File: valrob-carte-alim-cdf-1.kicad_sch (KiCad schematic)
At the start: 0 parts

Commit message: schem: add ESP32-S3-WROOM-1 MCU
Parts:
- added C5: 1u, Capacitor_SMD:C_0402_1005Metric, symbol Device:C
- added C6: 22u, Capacitor_SMD:C_0603_1608Metric, symbol Device:C
- added C7: 0u1, Capacitor_SMD:C_0402_1005Metric, symbol Device:C
- added J4, J6: Conn_01x04_Pin, Connector_PinHeader_2.54mm:PinHeader_1x04_P2.54mm_Vertical, symbol Connector:Conn_01x04_Pin
- added R6, R7: 10k, Resistor_SMD:R_0402_1005Metric, symbol Device:R
- added R8, R9: 22, Resistor_SMD:R_0402_1005Metric, symbol Device:R
- added U4: ESP32-S3-WROOM-1, PCM_Espressif:ESP32-S3-WROOM-1, symbol PCM_Espressif:ESP32-S3-WROOM-1
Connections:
- new net: J4.1 (Pin_1), U4.32 (MTCK/GPIO39/CLK_OUT3/SUBSPICS1)
- new net: J4.2 (Pin_2), U4.33 (MTDO/GPIO40/CLK_OUT2)
- new net: J4.3 (Pin_3), U4.34 (MTDI/GPIO41/CLK_OUT1)
- new net: J4.4 (Pin_4), U4.35 (MTMS/GPIO42)
- new net +3V3: C6.1, C7.1, J6.1 (Pin_1), R6.2, R7.2, U4.2 (3V3)
- new net BOOT: R7.1, U4.27 (GPIO0/BOOT)
- new net CHIP_PU: C5.2, R6.1, U4.3 (EN)
- new net D+: R8.2
- new net D-: R9.2
- new net ESP_D+: R8.1, U4.14 (GPIO20/U1CTS/ADC2_CH9/CLK_OUT1/USB_D+)
- new net ESP_D-: R9.1, U4.13 (GPIO19/U1RTS/ADC2_CH8/CLK_OUT2/USB_D-)
- new net GND: C5.1, C6.2, C7.2, J6.3 (Pin_3), U4.1 (GND), U4.40 (GND), U4.41 (GND)
- new net U0RXD: J6.2 (Pin_2), U4.36 (U0RXD/GPIO44/CLK_OUT2)
- new net U0TXD: J6.4 (Pin_4), U4.37 (U0TXD/GPIO43/CLK_OUT1)
- no-connect marks 0 -> 9
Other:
- note added: "EN RC delay"
- note added: "UART"

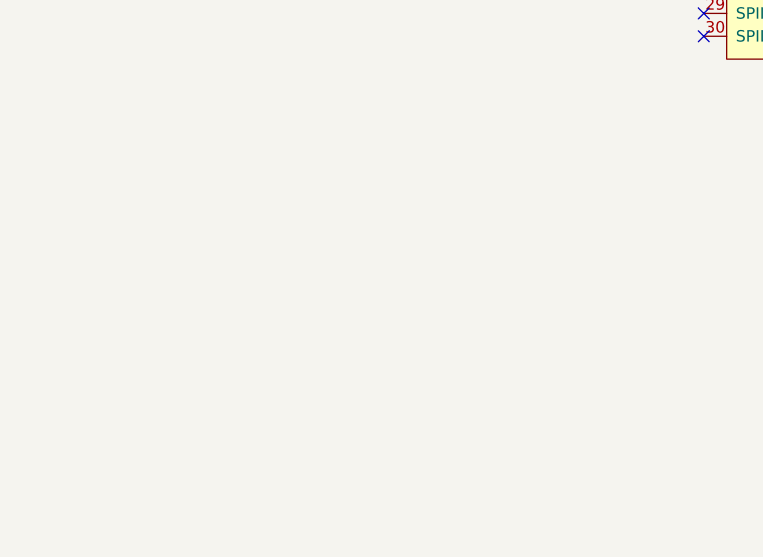
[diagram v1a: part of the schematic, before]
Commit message: schem: add USBC connector
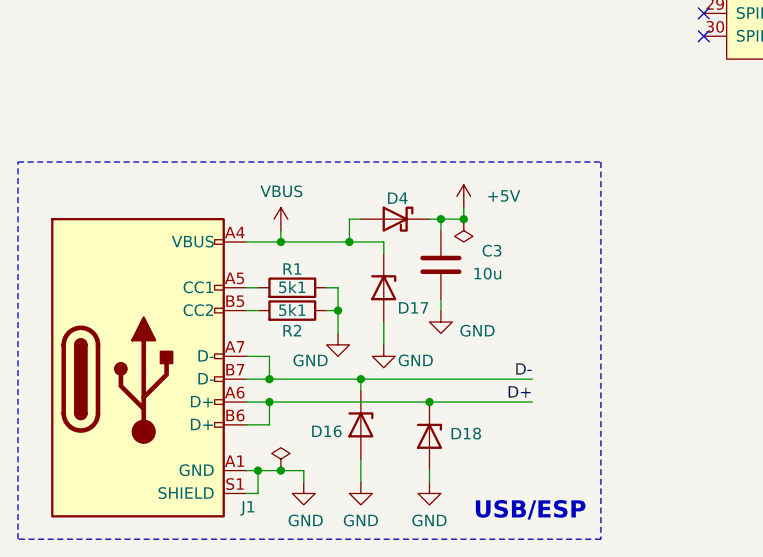
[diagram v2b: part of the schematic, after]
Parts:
- added C3: 10u, Capacitor_SMD:C_0603_1608Metric, symbol Device:C
- added D16, D17, D18: H5VU10U, Pers:Diode_DFN1006, symbol Pers:H5VU10U
- added D4: D_Schottky, Diode_SMD:D_SMA, symbol Device:D_Schottky
- added J1: USB_C_Receptacle_USB2.0_14P, Connector_USB:USB_C_Receptacle_HRO_TYPE-C-31-M-12, symbol Connector:USB_C_Receptacle_USB2.0_14P
- added R1, R2: 5k1, Resistor_SMD:R_0402_1005Metric, symbol Device:R
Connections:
- net D+: now also D18.1 (K), J1.A6 (D+), J1.B6 (D+)
- net D-: now also D16.1 (K), J1.A7 (D-), J1.B7 (D-)
- net GND: now also C3.2, D16.2 (A), D17.2 (A), D18.2 (A), J1.A1 (GND), J1.A12 (GND), J1.B1 (GND), J1.B12 (GND), J1.S1 (SHIELD), R1.1, R2.1
- new net: J1.A5 (CC1), R1.2
- new net: J1.B5 (CC2), R2.2
- new net +5V: C3.1, D4.1 (K)
- new net VBUS: D17.1 (K), D4.2 (A), J1.A4 (VBUS), J1.A9 (VBUS), J1.B4 (VBUS), J1.B9 (VBUS)
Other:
- note added: "USB/ESP"

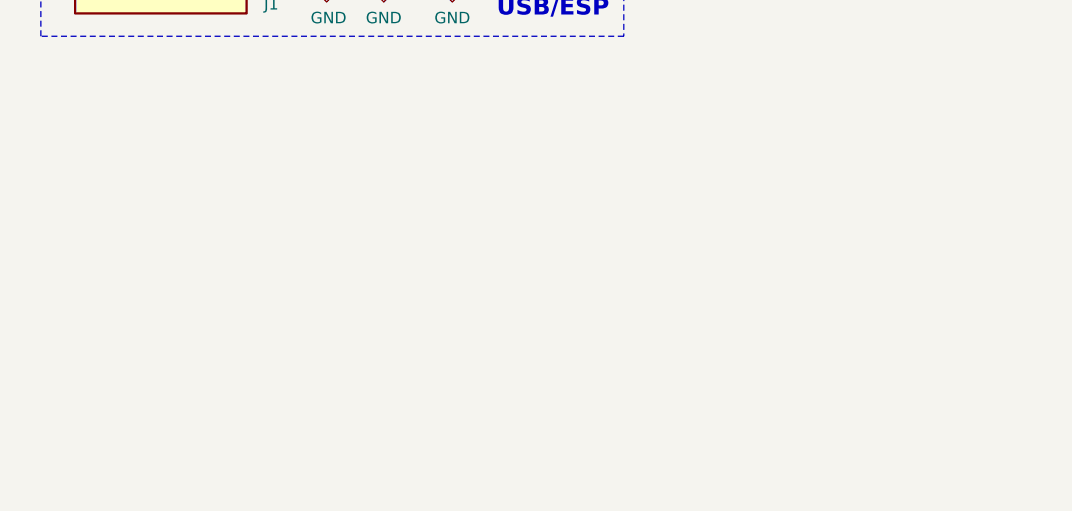
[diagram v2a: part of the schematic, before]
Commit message: schem: add TPS5430 5v logic SMPS
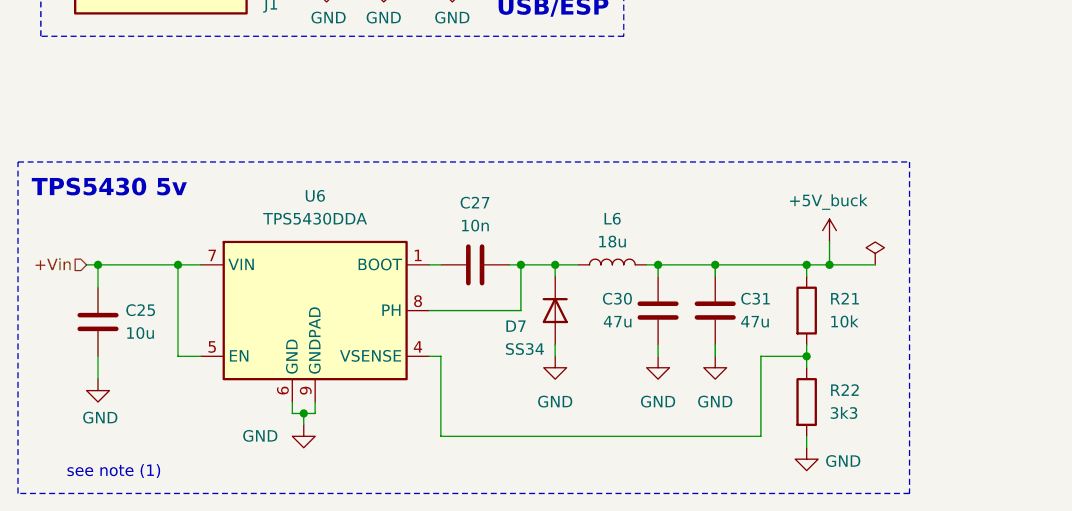
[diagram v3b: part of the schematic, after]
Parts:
- added C25: 10u, Capacitor_SMD:C_0805_2012Metric, symbol Device:C
- added C27: 10n, Capacitor_SMD:C_0402_1005Metric, symbol Device:C
- added C30, C31: 47u, Capacitor_SMD:C_1206_3216Metric, symbol Device:C
- added D7: SS34, Diode_SMD:D_SMA, symbol Device:D
- added L6: 18u, Inductor_SMD:L_Sunlord_SWRB1207S, symbol Device:L
- added R21: 10k, Resistor_SMD:R_0402_1005Metric, symbol Device:R
- added R22: 3k3, Resistor_SMD:R_0402_1005Metric, symbol Device:R
- added U6: TPS5430DDA, Package_SO:TI_SO-PowerPAD-8_ThermalVias, symbol Regulator_Switching:TPS5430DDA
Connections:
- net GND: now also C25.2, C30.2, C31.2, D7.2 (A), R22.2, U6.6 (GND), U6.9 (GNDPAD)
- new net: C27.2, D7.1 (K), L6.1, U6.8 (PH)
- new net: C27.1, U6.1 (BOOT)
- new net: R21.2, R22.1, U6.4 (VSENSE)
- new net +5V_buck: C30.1, C31.1, L6.2, R21.1
- new net +Vin: C25.1, U6.5 (EN), U6.7 (VIN)
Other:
- note added: "TPS5430 5v"
- note added: "see note (1)"

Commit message: schem: moved TSP5430 to power sheet
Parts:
- removed C25: 10u, Capacitor_SMD:C_0805_2012Metric, symbol Device:C
- removed C27: 10n, Capacitor_SMD:C_0402_1005Metric, symbol Device:C
- removed C30, C31: 47u, Capacitor_SMD:C_1206_3216Metric, symbol Device:C
- removed D7: SS34, Diode_SMD:D_SMA, symbol Device:D
- removed L6: 18u, Inductor_SMD:L_Sunlord_SWRB1207S, symbol Device:L
- removed R21: 10k, Resistor_SMD:R_0402_1005Metric, symbol Device:R
- removed R22: 3k3, Resistor_SMD:R_0402_1005Metric, symbol Device:R
- removed U6: TPS5430DDA, Package_SO:TI_SO-PowerPAD-8_ThermalVias, symbol Regulator_Switching:TPS5430DDA
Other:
- added sheet Power (power.kicad_sch)
- note removed: "TPS5430 5v"
- note removed: "see note (1)"

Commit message: schem: add BOOT and CHIP_PU btns
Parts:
- added SW1, SW2: SW_Push, Button_Switch_SMD:SW_SPST_TS-1088-xR020, symbol Switch:SW_Push
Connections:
- net BOOT: now also SW1.2
- net CHIP_PU: now also SW2.2
- net GND: now also SW1.1, SW2.1
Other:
- note added: "Buttons"

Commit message: schem: add TPS56A37 5V SMPS
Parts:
- C7: JLCPCB Part # C1525 -> C307331; Manufacturer Part Number CL05B104KO5NNNC -> CL05B104KB54PNC
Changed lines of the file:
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@@
 			)
 		)
-		(property "JLCPCB Part #" "C1525"
+		(property "JLCPCB Part #" "C307331"
 			(at 127 52.07 0)
 			(effects
@@
 			)
 		)
-		(property "Manufacturer Part Number" "CL05B104KO5NNNC"
+		(property "Manufacturer Part Number" "CL05B104KB54PNC"
 			(at 127 52.07 0)
 			(effects

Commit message: schem: add VBUS TO +5V jumper
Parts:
- added JP1: Jumper_2_Small_Open, Connector_PinHeader_2.54mm:PinHeader_2x01_P2.54mm_Vertical, symbol Jumper:Jumper_2_Small_Open
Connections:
- net VBUS: now also JP1.1 (A); no longer D4.2 (A)
- new net: D4.2 (A), JP1.2 (B)
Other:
- added sheet Connectors (connectors.kicad_sch)
- moved on the sheet: C3, D4
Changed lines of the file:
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@@
 	)
 	(junction
-		(at 64.77 160.02)
+		(at 71.12 160.02)
 		(diameter 0)
 		(color 0 0 0 0)
@@
 	)
 	(junction
-		(at 62.23 160.02)
+		(at 68.58 160.02)
 		(diameter 0)
 		(color 0 0 0 0)
@@
 	(wire
 		(pts
-			(xy 86.36 185.42) (xy 86.36 179.07)
+			(xy 52.07 160.02) (xy 53.34 160.02)
 		)
 		(stroke
@@
 	(wire
 		(pts
-			(xy 62.23 160.02) (xy 62.23 161.29)
+			(xy 86.36 185.42) (xy 86.36 179.07)
 		)
 		(stroke
@@
 	(wire
 		(pts
-			(xy 137.16 44.45) (xy 137.16 63.5)
+			(xy 68.58 160.02) (xy 68.58 161.29)
 		)
 		(stroke
@@
 	(wire
 		(pts
-			(xy 182.88 78.74) (xy 191.77 78.74)
+			(xy 137.16 44.45) (xy 137.16 63.5)
 		)
 		(stroke
@@
 	(wire
 		(pts
-			(xy 52.07 160.02) (xy 53.34 160.02)
+			(xy 182.88 78.74) (xy 191.77 78.74)
 		)
 		(stroke
@@
 	(wire
 		(pts
-			(xy 62.23 170.18) (xy 62.23 168.91)
+			(xy 68.58 170.18) (xy 68.58 168.91)
 		)
 		(stroke
@@
 	(wire
 		(pts
+			(xy 58.42 160.02) (xy 59.69 160.02)
+		)
+		(stroke
+			(width 0)
+			(type default)
+		)
+	)
+	(wire
+		(pts
 			(xy 40.64 175.26) (xy 43.18 175.26)
 		)
@@
 	(wire
 		(pts
-			(xy 64.77 160.02) (xy 62.23 160.02)
+			(xy 71.12 160.02) (xy 68.58 160.02)
 		)
 		(stroke
@@
 	(wire
 		(pts
-			(xy 62.23 160.02) (xy 60.96 160.02)
+			(xy 68.58 160.02) (xy 67.31 160.02)
 		)
 		(stroke
@@
 	(wire
 		(pts
-			(xy 64.77 160.02) (xy 64.77 158.75)
+			(xy 71.12 160.02) (xy 71.12 158.75)
 		)
 		(stroke
@@
 	(symbol
 		(lib_id "Device:C")
-		(at 62.23 165.1 0)
+		(at 68.58 165.1 0)
 		(mirror y)
 		(unit 1)
@@
 		(dnp no)
 		(property "Reference" "C3"
-			(at 69.088 163.576 0)
+			(at 75.438 163.576 0)
 			(effects
 				(font
@@
 		)
 		(property "Value" "10u"
-			(at 69.088 166.116 0)
+			(at 75.438 166.116 0)
 			(effects
 				(font
@@
 		)
 		(property "Footprint" "Capacitor_SMD:C_0603_1608Metric"
-			(at 61.2648 168.91 0)
+			(at 67.6148 168.91 0)
 			(effects
 				(font
@@
 		)
 		(property "Datasheet" "~"
-			(at 62.23 165.1 0)
+			(at 68.58 165.1 0)
 			(effects
 				(font
@@
 		)
 		(property "Description" "Unpolarized capacitor"
-			(at 62.23 165.1 0)
+			(at 68.58 165.1 0)
 			(effects
 				(font
@@
 		)
 		(property "Manufacturer" "Samsung Electro-Mechanics "
-			(at 62.23 165.1 0)
+			(at 68.58 165.1 0)
 			(effects
 				(font
@@
 		)
 		(property "Manufacturer Part Number" "CL10A106KP8NNNC"
-			(at 62.23 165.1 0)
+			(at 68.58 165.1 0)
 			(effects
 				(font
@@
 		)
 		(property "Basic" "Y"
-			(at 62.23 165.1 0)
+			(at 68.58 165.1 0)
 			(effects
 				(font
@@
 		)
 		(property "JLCPCB Part #" "C19702"
-			(at 62.23 165.1 0)
+			(at 68.58 165.1 0)
 			(effects
 				(font
@@
 	(symbol
 		(lib_id "power:GND")
-		(at 62.23 170.18 0)
+		(at 68.58 170.18 0)
 		(mirror y)
 		(unit 1)
@@
 		(dnp no)
 		(property "Reference" "#PWR011"
-			(at 62.23 176.53 0)
+			(at 68.58 176.53 0)
 			(effects
 				(font
@@
 		)
 		(property "Value" "GND"
-			(at 66.294 172.466 0)
+			(at 72.644 172.466 0)
 			(effects
 				(font
@@
 		)
 		(property "Footprint" ""
-			(at 62.23 170.18 0)
+			(at 68.58 170.18 0)
 			(effects
 				(font
@@
 		)
 		(property "Datasheet" ""
-			(at 62.23 170.18 0)
+			(at 68.58 170.18 0)
 			(effects
 				(font
@@
 		)
 		(property "Description" "Power symbol creates a global label with name \"GND\" , ground"
-			(at 62.23 170.18 0)
+			(at 68.58 170.18 0)
 			(effects
 				(font
@@
 	(symbol
 		(lib_id "power:PWR_FLAG")
-		(at 64.77 160.02 180)
+		(at 71.12 160.02 180)
 		(unit 1)
 		(exclude_from_sim no)
@@
 		(fields_autoplaced yes)
 		(property "Reference" "#FLG02"
-			(at 64.77 161.925 0)
+			(at 71.12 161.925 0)
 			(effects
 				(font
@@
 		)
 		(property "Value" "PWR_FLAG"
-			(at 64.77 165.1 0)
+			(at 71.12 165.1 0)
 			(effects
 				(font
@@
 		)
 		(property "Footprint" ""
-			(at 64.77 160.02 0)
+			(at 71.12 160.02 0)
 			(effects
 				(font
@@
 		)
 		(property "Datasheet" "~"
-			(at 64.77 160.02 0)
+			(at 71.12 160.02 0)
 			(effects
 				(font
@@
 		)
 		(property "Description" "Special symbol for telling ERC where power comes from"
-			(at 64.77 160.02 0)
+			(at 71.12 160.02 0)
 			(effects
 				(font
@@
 	)
 	(symbol
+		(lib_id "Jumper:Jumper_2_Small_Open")
+		(at 55.88 160.02 0)
+		(unit 1)
+		(exclude_from_sim no)
+		(in_bom yes)
+		(on_board yes)
+		(dnp no)
+		(fields_autoplaced yes)
+		(property "Reference" "JP1"
+			(at 55.88 156.21 0)
+			(effects
+				(font
+					(size 1.27 1.27)
+				)
+			)
+		)
+		(property "Value" "Jumper_2_Small_Open"
+			(at 55.88 156.21 0)
+			(effects
+				(font
+					(size 1.27 1.27)
+				)
+				(hide yes)
+			)
+		)
+		(property "Footprint" "Connector_PinHeader_2.54mm:PinHeader_2x01_P2.54mm_Vertical"
+			(at 55.88 160.02 0)
+			(effects
+				(font
+					(size 1.27 1.27)
+				)
+				(hide yes)
+			)
+		)
+		(property "Datasheet" "~"
+			(at 55.88 160.02 0)
+			(effects
+				(font
+					(size 1.27 1.27)
+				)
+				(hide yes)
+			)
+		)
+		(property "Description" "Jumper, 2-pole, small symbol, open"
+			(at 55.88 160.02 0)
+			(effects
+				(font
+					(size 1.27 1.27)
+				)
+				(hide yes)
+			)
+		)
+		(pin "2"
+		)
+		(pin "1"
+		)
+		(instances
+			(project ""
+				(path "/8d7b287d-627f-46aa-8c27-0b5ed29ab4a2"
+					(reference "JP1")
+					(unit 1)
+				)
+			)
+		)
+	)
+	(symbol
 		(lib_id "power:GND")
 		(at 50.8 172.72 0)
@@
 	(symbol
 		(lib_id "Device:D_Schottky")
-		(at 57.15 160.02 0)
+		(at 63.5 160.02 0)
 		(mirror y)
 		(unit 1)
@@
 		(dnp no)
 		(property "Reference" "D4"
-			(at 57.404 157.734 0)
+			(at 63.754 157.734 0)
 			(effects
 				(font
@@
 		)
 		(property "Value" "D_Schottky"
-			(at 57.4675 156.21 0)
+			(at 63.8175 156.21 0)
 			(effects
 				(font
@@
 		)
 		(property "Footprint" "Diode_SMD:D_SMA"
-			(at 57.15 160.02 0)
+			(at 63.5 160.02 0)
 			(effects
 				(font
@@
 		)
 		(property "Datasheet" "~"
-			(at 57.15 160.02 0)
+			(at 63.5 160.02 0)
 			(effects
 				(font
@@
 		)
 		(property "Description" "Schottky diode"
-			(at 57.15 160.02 0)
+			(at 63.5 160.02 0)
 			(effects
 				(font
@@
 		)
 		(property "Manufacturer" "Microdiode Semiconductor (MDD)"
-			(at 57.15 160.02 0)
+			(at 63.5 160.02 0)
 			(effects
 				(font
@@
 		)
 		(property "Manufacturer Part Number" "SS54"
-			(at 57.15 160.02 0)
+			(at 63.5 160.02 0)
 			(effects
 				(font
@@
 		)
 		(property "Basic" "Y"
-			(at 57.15 160.02 0)
+			(at 63.5 160.02 0)
 			(effects
 				(font
@@
 		)
 		(property "JLCPCB Part #" "C22452"
-			(at 57.15 160.02 0)
+			(at 63.5 160.02 0)
 			(effects
 				(font
@@
 	(symbol
 		(lib_id "power:+5V")
-		(at 64.77 158.75 0)
+		(at 71.12 158.75 0)
 		(mirror y)
 		(unit 1)
@@
 		(fields_autoplaced yes)
 		(property "Reference" "#PWR012"
-			(at 64.77 162.56 0)
+			(at 71.12 162.56 0)
 			(effects
 				(font
@@
 		)
 		(property "Value" "+5V"
-			(at 67.31 157.4799 0)
+			(at 73.66 157.4799 0)
 			(effects
 				(font
@@
 		)
 		(property "Footprint" ""
-			(at 64.77 158.75 0)
+			(at 71.12 158.75 0)
 			(effects
 				(font
@@
 		)
 		(property "Datasheet" ""
-			(at 64.77 158.75 0)
+			(at 71.12 158.75 0)
 			(effects
 				(font
@@
 		)
 		(property "Description" "Power symbol creates a global label with name \"+5V\""
-			(at 64.77 158.75 0)
+			(at 71.12 158.75 0)
 			(effects
 				(font
@@
 				)
 			)
+		)
+	)
+	(sheet
+		(at 198.12 142.24)
+		(size 12.7 15.24)
+		(exclude_from_sim no)
+		(in_bom yes)
+		(on_board yes)
+		(dnp no)
+		(fields_autoplaced yes)
+		(stroke
+			(width 0.1524)
+			(type solid)
+		)
+		(fill
+			(color 0 0 0 0.0000)
+		)
+		(property "Sheetname" "Connectors"
+			(at 198.12 141.5284 0)
+			(effects
+				(font
+					(size 1.27 1.27)
+				)
+				(justify left bottom)
+			)
+		)
+		(property "Sheetfile" "connectors.kicad_sch"
+			(at 198.12 158.0646 0)
+			(effects
+				(font
+					(size 1.27 1.27)
+				)
+				(justify left top)
+			)
+		)
+		(instances
+			(project "valrob-carte-alim-cdf-1"
+				(path "/8d7b287d-627f-46aa-8c27-0b5ed29ab4a2"
+					(page "5")
+				)
+			)

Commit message: schem: add ILM pins and 12V 10A rail
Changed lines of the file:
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@@
 	)
 	(sheet
-		(at 227.33 115.57)
+		(at 227.33 139.7)
 		(size 17.78 17.78)
 		(exclude_from_sim no)
@@
 		)
 		(property "Sheetname" "Power"
-			(at 227.33 114.8584 0)
+			(at 227.33 138.9884 0)
 			(effects
 				(font
@@
 		)
 		(property "Sheetfile" "power.kicad_sch"
-			(at 227.33 133.9346 0)
+			(at 227.33 158.0646 0)
 			(effects
 				(font
